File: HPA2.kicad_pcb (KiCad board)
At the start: 2 copper layers, 101.6 x 73 mm, 120 parts, among them J1 Input, J2 Conn_01x01_Male, J3 Power, J4 Output, J5 Mute, K1 G6H-2, Q1 BC560C, Q10 BC560C, Q11 BC560C, Q12 BC550C, Q13 BC550C, Q14 KSC1845, Q15 BC550C, Q16 BC560C, Q17 KSA992, Q18 BC560C, Q19 BC550C, Q2 BC560C, Q20 BC560C, Q21 BC550C, Q22 TTA004B, Q23 TTA004B, Q24 TTC004B, Q25 TTC004B, Q26 KSC2690AY, Q27 KSA1220AY, Q3 BC549C, Q4 BC549C, Q5 BC549C, Q6 BC560C, Q7 BC549C, Q8 BC560C, Q9 BC560C, U1 2N5564, U2 LT1761-BYP, U3 LT1964-BYP, U4 ADA4627-1

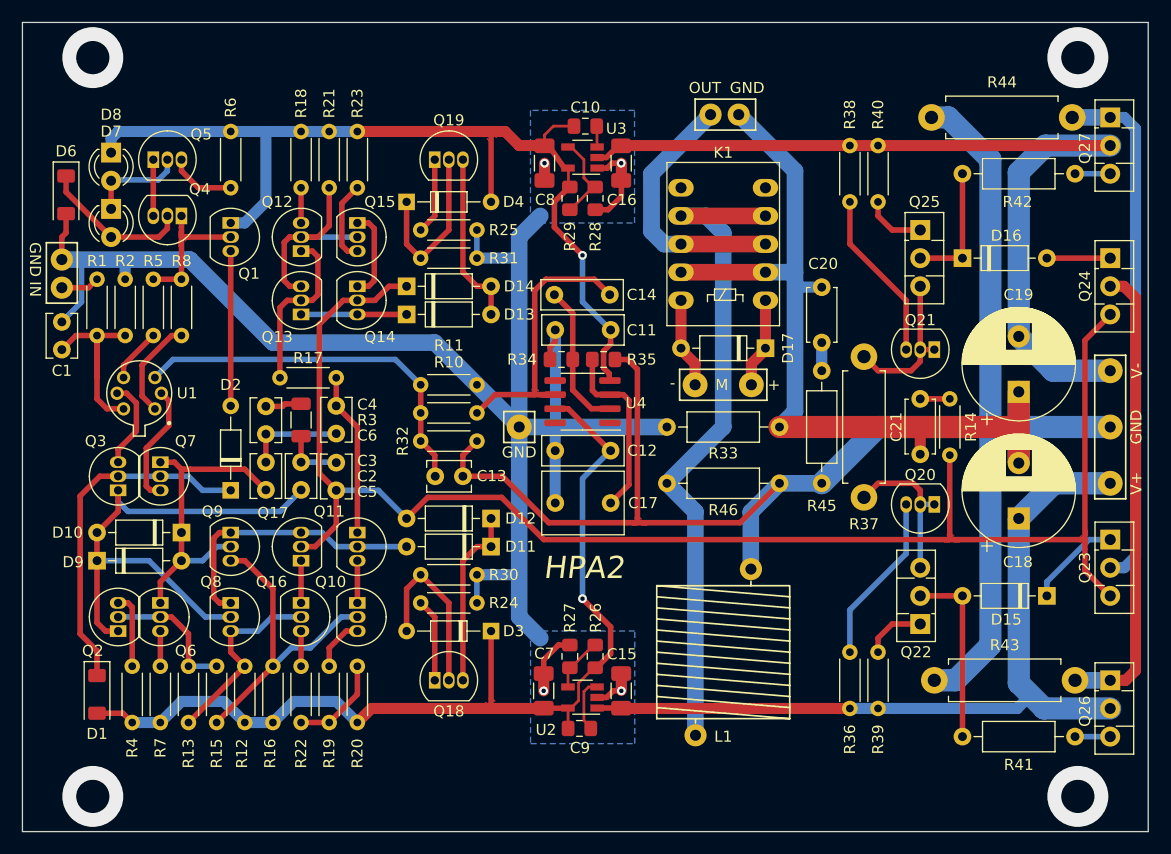
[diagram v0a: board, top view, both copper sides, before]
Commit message: - Removed useless triangular copper pours at trace butt joints - Separated footprints of thermally connected transistor pairs to fix DRC warnings
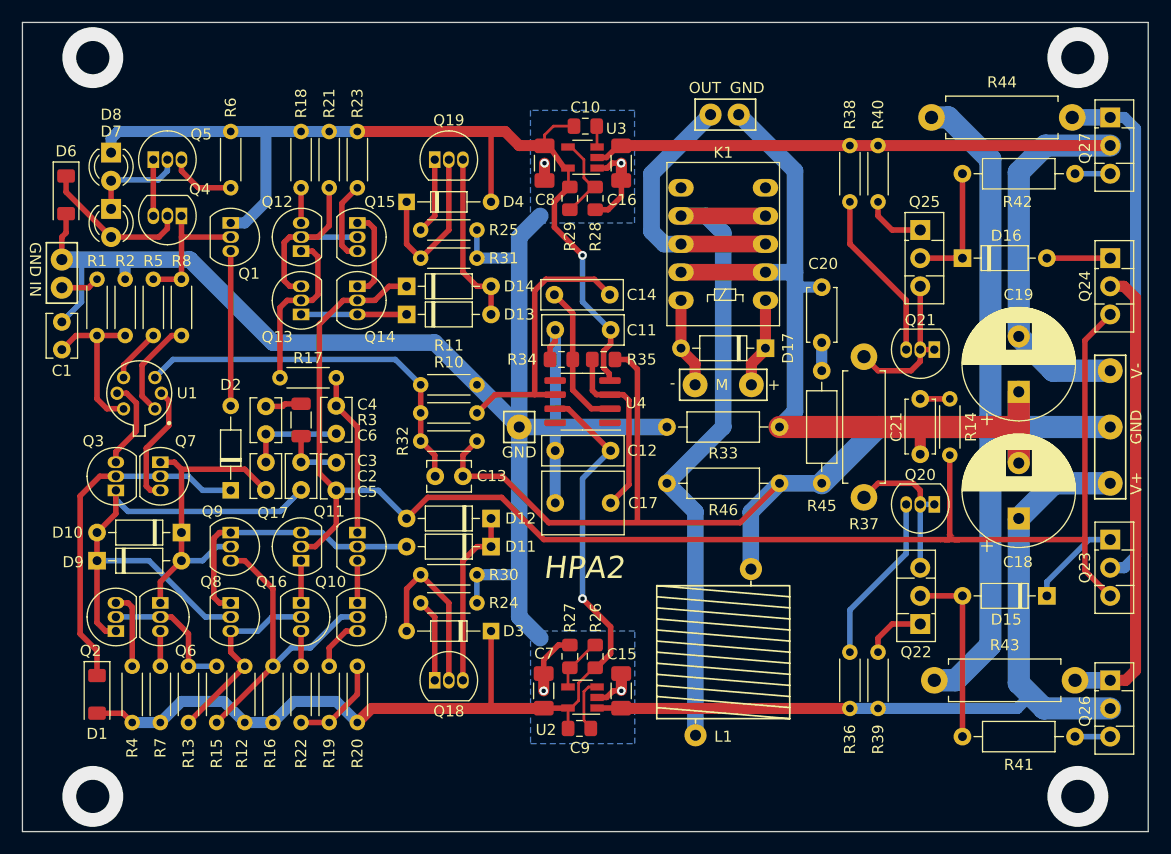
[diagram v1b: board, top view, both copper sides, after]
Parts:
- moved Q3 0.21 mm to (90.6, 112.4)
- moved Q2 0.21 mm to (90.6, 125.1)
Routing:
- net Net-(C1-Pad1): track 18.5 -> 14.7 mm
- net Net-(C14-Pad2): track 26.1 -> 24.9 mm
- removed copper zone on F.Cu, net Net-(C13-Pad1)
- removed copper zone on F.Cu, net Net-(C14-Pad2)
- removed copper zone on F.Cu, net Net-(C3-Pad2)
- removed copper zone on F.Cu, net Net-(Q1-Pad2)
- removed copper zone on F.Cu, net Vreg+
- removed copper zone on F.Cu, net Vreg-

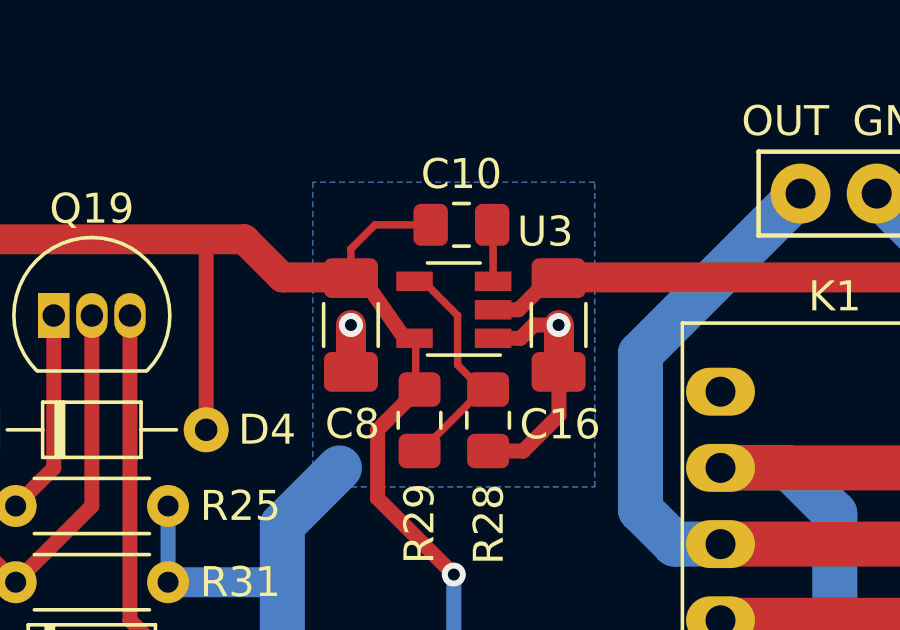
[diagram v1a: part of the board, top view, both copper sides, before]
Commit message: Loaded the existing TSOT-23-5 footprint from the board and saved it to the project-local footprint library. Updated the board. This prevents breaking the U2 regulator layout when updating from latest footprint libraries.
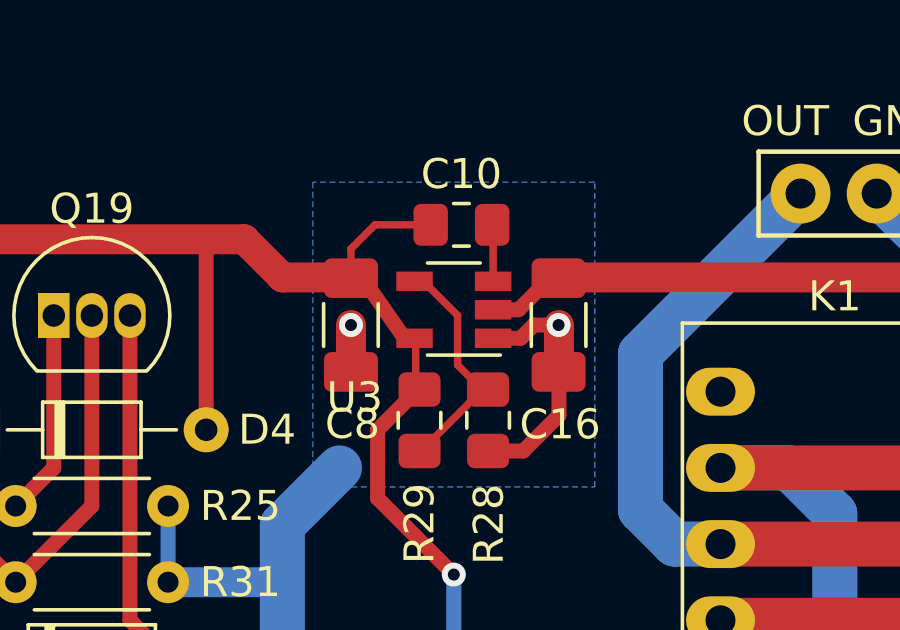
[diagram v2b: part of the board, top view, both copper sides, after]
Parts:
- U2, U3: footprint Package_TO_SOT_SMD:TSOT-23-5 -> HPA2-footprints:TSOT-23-5
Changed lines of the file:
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@@
 		)
 	)
-	(footprint "Package_TO_SOT_SMD:TSOT-23-5"
+	(footprint "HPA2-footprints:TSOT-23-5"
 		(layer "F.Cu")
 		(at 132.715 82.3595 180)
@@
 		(tags "TSOT-23-5")
 		(property "Reference" "U3"
-			(at -3.048 2.6035 180)
+			(at 3.302 -2.921 180)
 			(layer "F.SilkS")
 			(effects
@@
 		)
 	)
-	(footprint "Package_TO_SOT_SMD:TSOT-23-5"
+	(footprint "HPA2-footprints:TSOT-23-5"
 		(layer "F.Cu")
 		(at 132.715 131.0894 180)

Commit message: Copied the HPA-Output-Coil footprint to the project-local library and updated the board.
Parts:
- L1: footprint HP_Footprints:HPA-Output-Coil -> HPA2-footprints:HPA-Output-Coil
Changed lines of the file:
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@@
 		)
 	)
-	(footprint "HP_Footprints:HPA-Output-Coil"
+	(footprint "HPA2-footprints:HPA-Output-Coil"
 		(layer "F.Cu")
 		(at 145.415 127 90)
@@
 		)
 		(fp_line
+			(start -8.7 6.2)
+			(end -8.7 -6.3)
+			(stroke
+				(width 0.12)
+				(type solid)
+			)
+			(layer "F.CrtYd")
+		)
+		(fp_line
 			(start 8.7 6.3)
 			(end -8.7 6.3)
 			(stroke
 				(width 0.12)
-				(type solid)
-			)
-			(layer "F.CrtYd")
-		)
-		(fp_line
-			(start -8.7 6.3)
-			(end -8.7 -6.3)
-			(stroke
-				(width 0.12)

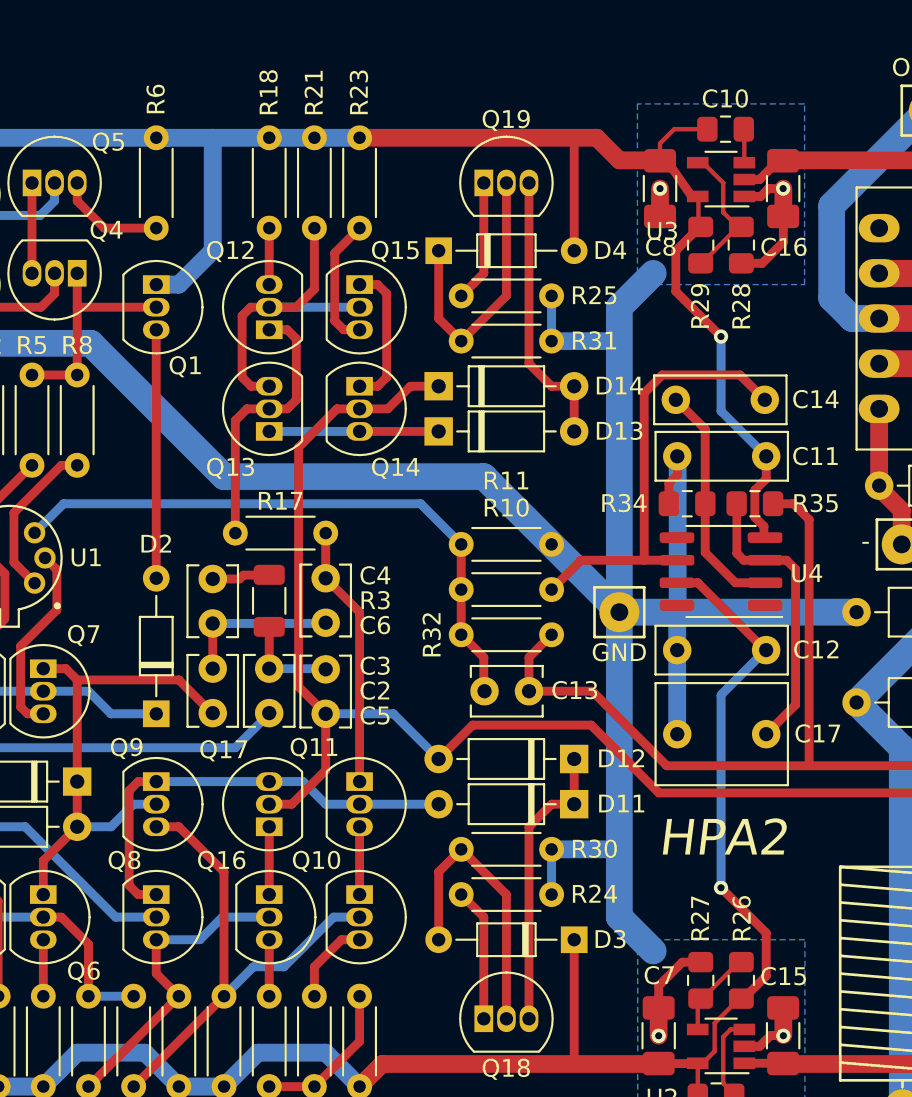
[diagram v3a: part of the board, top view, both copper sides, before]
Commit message: Updated DO-34 footprint to move "K" silkscreen to f-fab, and made sure the footprint is in the porject-local library.  Updated board.
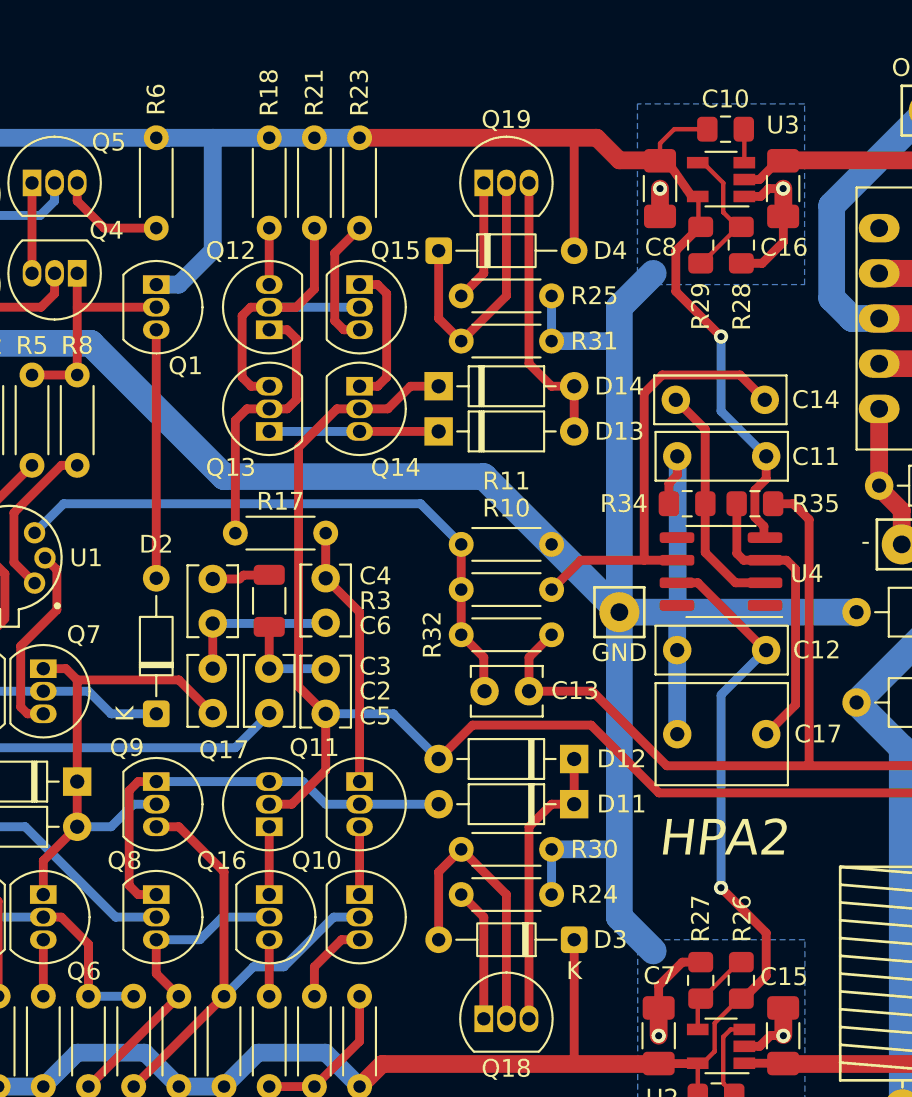
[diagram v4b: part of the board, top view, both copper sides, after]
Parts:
- D2, D3, D4: footprint Diode_THT:D_DO-34_SOD68_P7.62mm_Horizontal -> HPA2-footprints:D_DO-34_SOD68_P7.62mm_Horizontal
